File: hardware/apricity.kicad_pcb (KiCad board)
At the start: 2 copper layers, 71.2 x 71.2 mm, 26 parts, among them J1 USB_C_Receptacle_USB2.0, U1 ESP-WROOM-02D, U2 X

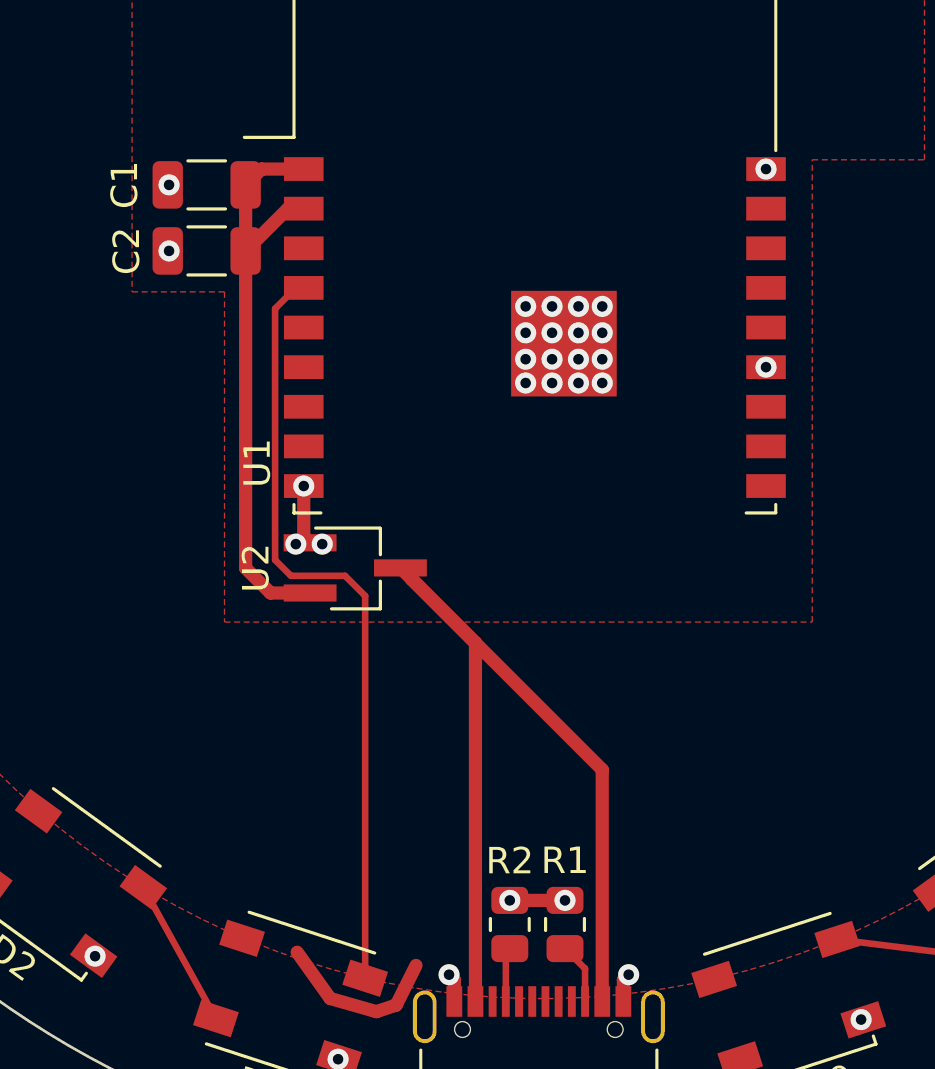
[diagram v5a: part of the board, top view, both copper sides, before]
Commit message: remove vias from under pads
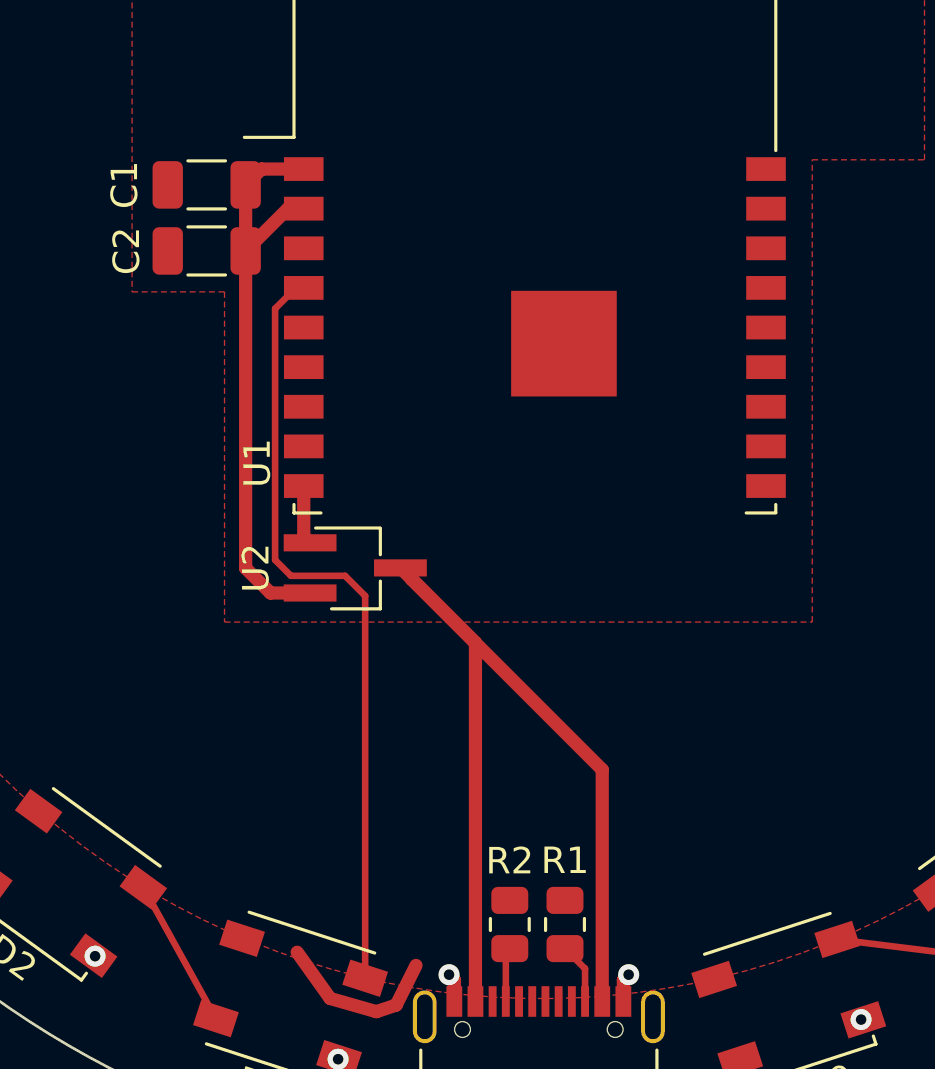
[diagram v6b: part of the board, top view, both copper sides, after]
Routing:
- net GND: track 6.54 -> 4.45 mm, vias 46 -> 21
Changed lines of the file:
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@@
   )
   (segment (start 139 103.6) (end 139 105.51) (width 0.5) (layer "F.Cu") (net 1))
-  (segment (start 146.8 119.2875) (end 148.89 119.2875) (width 0.5) (layer "F.Cu") (net 1))
   (segment (start 144.7 122.3) (end 144.5 122.1) (width 0.5) (layer "F.Cu") (net 1))
   (segment (start 151.1 122.3) (end 151.3 122.1) (width 0.5) (layer "F.Cu") (net 1))
@@
   (segment (start 139 105.51) (end 139.24 105.75) (width 0.5) (layer "F.Cu") (net 1))
   (via (at 155.7 62.7) (size 0.8) (drill 0.4) (layers "F.Cu" "B.Cu") (net 1))
-  (via (at 150.3 96.8) (size 0.8) (drill 0.4) (layers "F.Cu" "B.Cu") (net 1))
-  (via (at 147.4 98.8) (size 0.8) (drill 0.4) (layers "F.Cu" "B.Cu") (net 1))
-  (via (at 148.4 96.8) (size 0.8) (drill 0.4) (layers "F.Cu" "B.Cu") (net 1))
   (via (at 144.5 122.1) (size 0.8) (drill 0.4) (layers "F.Cu" "B.Cu") (free) (net 1))
-  (via (at 147.4 96.8) (size 0.8) (drill 0.4) (layers "F.Cu" "B.Cu") (net 1))
-  (via (at 150.3 97.8) (size 0.8) (drill 0.4) (layers "F.Cu" "B.Cu") (net 1))
   (via (at 135.8 64.2) (size 0.8) (drill 0.4) (layers "F.Cu" "B.Cu") (net 1))
-  (via (at 150.3 98.8) (size 0.8) (drill 0.4) (layers "F.Cu" "B.Cu") (net 1))
   (via (at 177.8 81.8) (size 0.8) (drill 0.4) (layers "F.Cu" "B.Cu") (net 1))
   (via (at 172.6 73.2) (size 0.8) (drill 0.4) (layers "F.Cu" "B.Cu") (net 1))
   (via (at 179.3 101.7) (size 0.8) (drill 0.4) (layers "F.Cu" "B.Cu") (net 1))
-  (via (at 133.9 94.7) (size 0.8) (drill 0.4) (layers "F.Cu" "B.Cu") (net 1))
-  (via (at 146.8 119.2875) (size 0.8) (drill 0.4) (layers "F.Cu" "B.Cu") (net 1))
-  (via (at 156.5 91.6) (size 0.8) (drill 0.4) (layers "F.Cu" "B.Cu") (net 1))
   (via (at 165 66.6) (size 0.8) (drill 0.4) (layers "F.Cu" "B.Cu") (net 1))
-  (via (at 133.9 92.2) (size 0.8) (drill 0.4) (layers "F.Cu" "B.Cu") (net 1))
-  (via (at 149.4 97.8) (size 0.8) (drill 0.4) (layers "F.Cu" "B.Cu") (net 1))
   (via (at 118.2 106.3) (size 0.8) (drill 0.4) (layers "F.Cu" "B.Cu") (net 1))
   (via (at 127.2 69.4) (size 0.8) (drill 0.4) (layers "F.Cu" "B.Cu") (net 1))
-  (via (at 139.7 105.8) (size 0.8) (drill 0.4) (layers "F.Cu" "B.Cu") (net 1))
   (via (at 168.8 118.6) (size 0.8) (drill 0.4) (layers "F.Cu" "B.Cu") (net 1))
   (via (at 145.6 61.9) (size 0.8) (drill 0.4) (layers "F.Cu" "B.Cu") (net 1))
-  (via (at 148.4 97.8) (size 0.8) (drill 0.4) (layers "F.Cu" "B.Cu") (net 1))
-  (via (at 148.89 119.2875) (size 0.8) (drill 0.4) (layers "F.Cu" "B.Cu") (net 1))
-  (via (at 139 103.6) (size 0.8) (drill 0.4) (layers "F.Cu" "B.Cu") (net 1))
-  (via (at 147.4 99.7) (size 0.8) (drill 0.4) (layers "F.Cu" "B.Cu") (net 1))
   (via (at 115.9 96.4) (size 0.8) (drill 0.4) (layers "F.Cu" "B.Cu") (net 1))
-  (via (at 148.4 98.8) (size 0.8) (drill 0.4) (layers "F.Cu" "B.Cu") (net 1))
   (via (at 151.3 122.1) (size 0.8) (drill 0.4) (layers "F.Cu" "B.Cu") (free) (net 1))
   (via (at 131.1 121.4) (size 0.8) (drill 0.4) (layers "F.Cu" "B.Cu") (net 1))
   (via (at 116.7 86.4) (size 0.8) (drill 0.4) (layers "F.Cu" "B.Cu") (net 1))
-  (via (at 150.3 99.7) (size 0.8) (drill 0.4) (layers "F.Cu" "B.Cu") (net 1))
   (via (at 175.4 111) (size 0.8) (drill 0.4) (layers "F.Cu" "B.Cu") (net 1))
-  (via (at 138.7 105.8) (size 0.8) (drill 0.4) (layers "F.Cu" "B.Cu") (net 1))
-  (via (at 148.4 99.7) (size 0.8) (drill 0.4) (layers "F.Cu" "B.Cu") (net 1))
-  (via (at 149.4 96.8) (size 0.8) (drill 0.4) (layers "F.Cu" "B.Cu") (net 1))
   (via (at 160.1 123.8) (size 0.8) (drill 0.4) (layers "F.Cu" "B.Cu") (net 1))
   (via (at 140.3 125.3) (size 0.8) (drill 0.4) (layers "F.Cu" "B.Cu") (net 1))
-  (via (at 147.4 97.8) (size 0.8) (drill 0.4) (layers "F.Cu" "B.Cu") (net 1))
   (via (at 120.6 77) (size 0.8) (drill 0.4) (layers "F.Cu" "B.Cu") (net 1))
-  (via (at 156.5 99.1) (size 0.8) (drill 0.4) (layers "F.Cu" "B.Cu") (net 1))
-  (via (at 149.4 98.8) (size 0.8) (drill 0.4) (layers "F.Cu" "B.Cu") (net 1))
   (via (at 180.1 91.6) (size 0.8) (drill 0.4) (layers "F.Cu" "B.Cu") (net 1))
-  (via (at 149.4 99.7) (size 0.8) (drill 0.4) (layers "F.Cu" "B.Cu") (net 1))
   (via (at 123.4 114.8) (size 0.8) (drill 0.4) (layers "F.Cu" "B.Cu") (net 1))
   (segment (start 150.3 123.115) (end 150.3 114.34) (width 0.5) (layer "F.Cu") (net 2))

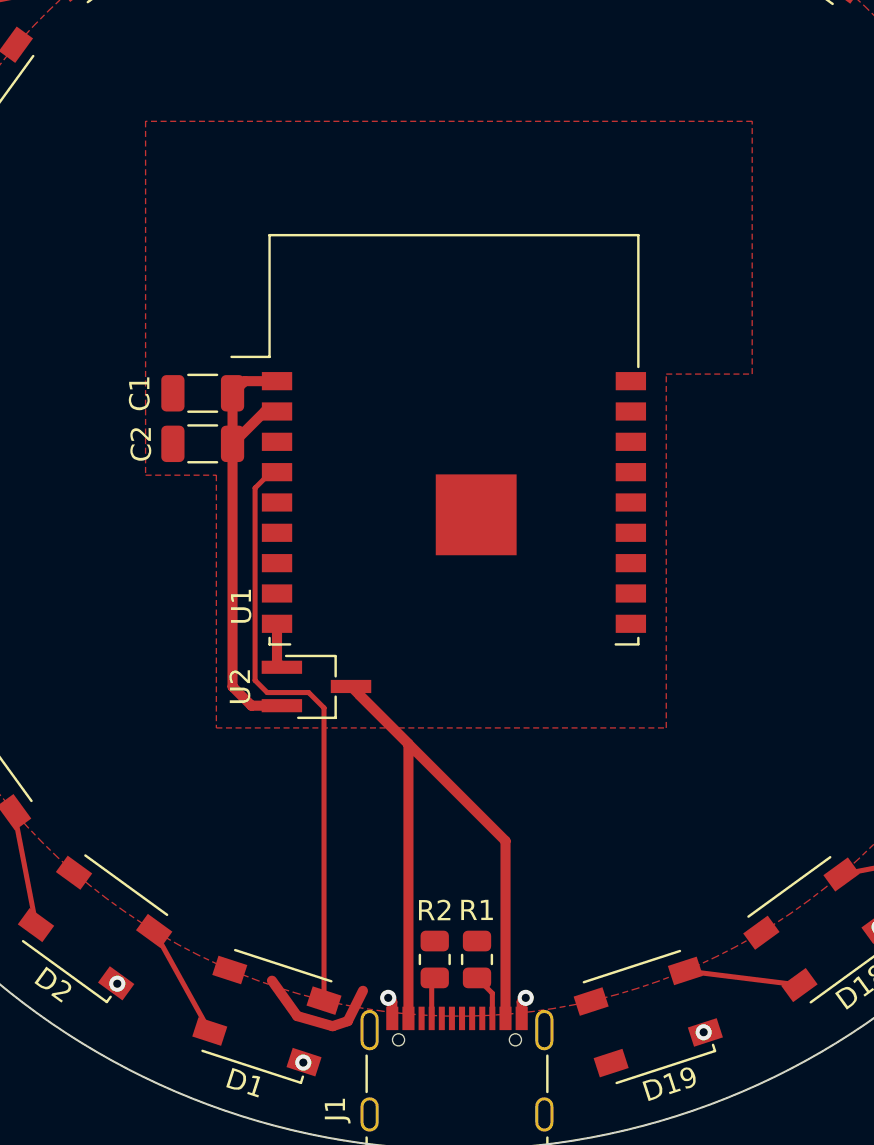
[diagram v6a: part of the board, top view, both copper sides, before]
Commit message: reintroduce ground plane below controller
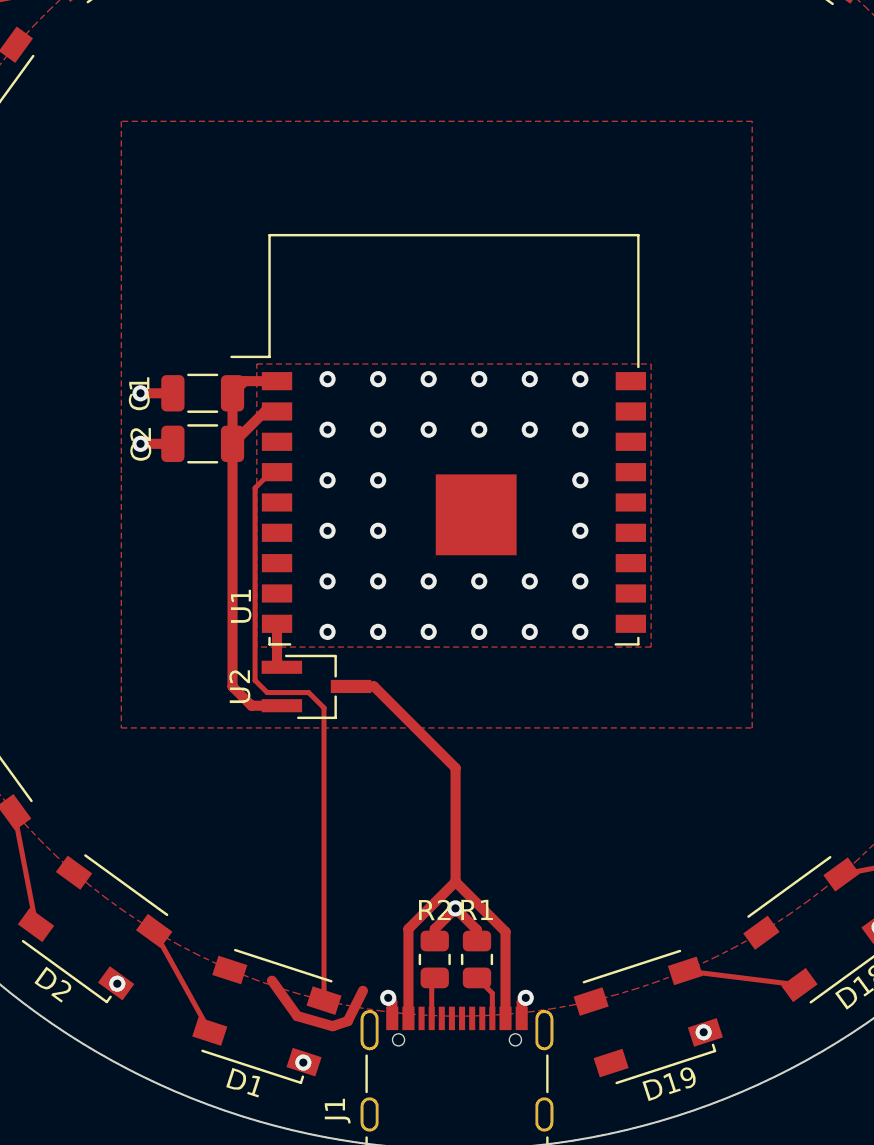
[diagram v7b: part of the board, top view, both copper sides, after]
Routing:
- net +5V: track 43.0 -> 34.4 mm
- net GND: track 4.45 -> 11.7 mm, vias 21 -> 54
- added copper zone on F.Cu, net GND
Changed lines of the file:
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@@
   )
   (segment (start 139 103.6) (end 139 105.51) (width 0.5) (layer "F.Cu") (net 1))
+  (segment (start 133.85 92.2) (end 132.25 92.2) (width 0.5) (layer "F.Cu") (net 1))
+  (segment (start 133.85 94.7) (end 132.25 94.7) (width 0.5) (layer "F.Cu") (net 1))
+  (segment (start 146.8 118.7) (end 147.825 117.675) (width 0.5) (layer "F.Cu") (net 1))
+  (segment (start 148.89 119.2875) (end 148.89 118.74) (width 0.5) (layer "F.Cu") (net 1))
   (segment (start 144.7 122.3) (end 144.5 122.1) (width 0.5) (layer "F.Cu") (net 1))
+  (segment (start 148.89 118.74) (end 147.825 117.675) (width 0.5) (layer "F.Cu") (net 1))
+  (segment (start 146.8 119.2875) (end 146.8 118.7) (width 0.5) (layer "F.Cu") (net 1))
   (segment (start 151.1 122.3) (end 151.3 122.1) (width 0.5) (layer "F.Cu") (net 1))
   (segment (start 151.1 123.115) (end 151.1 122.3) (width 0.5) (layer "F.Cu") (net 1))
@@
   (segment (start 139 105.51) (end 139.24 105.75) (width 0.5) (layer "F.Cu") (net 1))
   (via (at 155.7 62.7) (size 0.8) (drill 0.4) (layers "F.Cu" "B.Cu") (net 1))
+  (via (at 147.825 117.675) (size 0.8) (drill 0.4) (layers "F.Cu" "B.Cu") (free) (net 1))
+  (via (at 154 99) (size 0.8) (drill 0.4) (layers "F.Cu" "B.Cu") (free) (net 1))
+  (via (at 146.5 94) (size 0.8) (drill 0.4) (layers "F.Cu" "B.Cu") (free) (net 1))
+  (via (at 149 101.5) (size 0.8) (drill 0.4) (layers "F.Cu" "B.Cu") (free) (net 1))
+  (via (at 132.25 92.2) (size 0.8) (drill 0.4) (layers "F.Cu" "B.Cu") (free) (net 1))
+  (via (at 149 94) (size 0.8) (drill 0.4) (layers "F.Cu" "B.Cu") (free) (net 1))
+  (via (at 144 94) (size 0.8) (drill 0.4) (layers "F.Cu" "B.Cu") (free) (net 1))
+  (via (at 144 101.5) (size 0.8) (drill 0.4) (layers "F.Cu" "B.Cu") (free) (net 1))
   (via (at 144.5 122.1) (size 0.8) (drill 0.4) (layers "F.Cu" "B.Cu") (free) (net 1))
   (via (at 135.8 64.2) (size 0.8) (drill 0.4) (layers "F.Cu" "B.Cu") (net 1))
+  (via (at 151.5 101.5) (size 0.8) (drill 0.4) (layers "F.Cu" "B.Cu") (free) (net 1))
   (via (at 177.8 81.8) (size 0.8) (drill 0.4) (layers "F.Cu" "B.Cu") (net 1))
   (via (at 172.6 73.2) (size 0.8) (drill 0.4) (layers "F.Cu" "B.Cu") (net 1))
   (via (at 179.3 101.7) (size 0.8) (drill 0.4) (layers "F.Cu" "B.Cu") (net 1))
   (via (at 165 66.6) (size 0.8) (drill 0.4) (layers "F.Cu" "B.Cu") (net 1))
+  (via (at 151.5 91.5) (size 0.8) (drill 0.4) (layers "F.Cu" "B.Cu") (free) (net 1))
+  (via (at 154 94) (size 0.8) (drill 0.4) (layers "F.Cu" "B.Cu") (free) (net 1))
   (via (at 118.2 106.3) (size 0.8) (drill 0.4) (layers "F.Cu" "B.Cu") (net 1))
   (via (at 127.2 69.4) (size 0.8) (drill 0.4) (layers "F.Cu" "B.Cu") (net 1))
+  (via (at 146.5 104) (size 0.8) (drill 0.4) (layers "F.Cu" "B.Cu") (free) (net 1))
+  (via (at 154 101.5) (size 0.8) (drill 0.4) (layers "F.Cu" "B.Cu") (free) (net 1))
   (via (at 168.8 118.6) (size 0.8) (drill 0.4) (layers "F.Cu" "B.Cu") (net 1))
   (via (at 145.6 61.9) (size 0.8) (drill 0.4) (layers "F.Cu" "B.Cu") (net 1))
+  (via (at 154 104) (size 0.8) (drill 0.4) (layers "F.Cu" "B.Cu") (free) (net 1))
+  (via (at 141.5 96.5) (size 0.8) (drill 0.4) (layers "F.Cu" "B.Cu") (free) (net 1))
+  (via (at 144 104) (size 0.8) (drill 0.4) (layers "F.Cu" "B.Cu") (free) (net 1))
+  (via (at 151.5 94) (size 0.8) (drill 0.4) (layers "F.Cu" "B.Cu") (free) (net 1))
+  (via (at 141.5 91.5) (size 0.8) (drill 0.4) (layers "F.Cu" "B.Cu") (free) (net 1))
+  (via (at 132.25 94.7) (size 0.8) (drill 0.4) (layers "F.Cu" "B.Cu") (free) (net 1))
   (via (at 115.9 96.4) (size 0.8) (drill 0.4) (layers "F.Cu" "B.Cu") (net 1))
+  (via (at 149 91.5) (size 0.8) (drill 0.4) (layers "F.Cu" "B.Cu") (free) (net 1))
+  (via (at 146.5 101.5) (size 0.8) (drill 0.4) (layers "F.Cu" "B.Cu") (free) (net 1))
   (via (at 151.3 122.1) (size 0.8) (drill 0.4) (layers "F.Cu" "B.Cu") (free) (net 1))
   (via (at 131.1 121.4) (size 0.8) (drill 0.4) (layers "F.Cu" "B.Cu") (net 1))
   (via (at 116.7 86.4) (size 0.8) (drill 0.4) (layers "F.Cu" "B.Cu") (net 1))
+  (via (at 144 99) (size 0.8) (drill 0.4) (layers "F.Cu" "B.Cu") (free) (net 1))
   (via (at 175.4 111) (size 0.8) (drill 0.4) (layers "F.Cu" "B.Cu") (net 1))
+  (via (at 144 96.5) (size 0.8) (drill 0.4) (layers "F.Cu" "B.Cu") (free) (net 1))
+  (via (at 144 91.5) (size 0.8) (drill 0.4) (layers "F.Cu" "B.Cu") (free) (net 1))
+  (via (at 149 104) (size 0.8) (drill 0.4) (layers "F.Cu" "B.Cu") (free) (net 1))
+  (via (at 154 96.5) (size 0.8) (drill 0.4) (layers "F.Cu" "B.Cu") (free) (net 1))
   (via (at 160.1 123.8) (size 0.8) (drill 0.4) (layers "F.Cu" "B.Cu") (net 1))
+  (via (at 141.5 99) (size 0.8) (drill 0.4) (layers "F.Cu" "B.Cu") (free) (net 1))
   (via (at 140.3 125.3) (size 0.8) (drill 0.4) (layers "F.Cu" "B.Cu") (net 1))
   (via (at 120.6 77) (size 0.8) (drill 0.4) (layers "F.Cu" "B.Cu") (net 1))
+  (via (at 151.5 104) (size 0.8) (drill 0.4) (layers "F.Cu" "B.Cu") (free) (net 1))
+  (via (at 154 91.5) (size 0.8) (drill 0.4) (layers "F.Cu" "B.Cu") (free) (net 1))
   (via (at 180.1 91.6) (size 0.8) (drill 0.4) (layers "F.Cu" "B.Cu") (net 1))
+  (via (at 141.5 104) (size 0.8) (drill 0.4) (layers "F.Cu" "B.Cu") (free) (net 1))
+  (via (at 141.5 94) (size 0.8) (drill 0.4) (layers "F.Cu" "B.Cu") (free) (net 1))
   (via (at 123.4 114.8) (size 0.8) (drill 0.4) (layers "F.Cu" "B.Cu") (net 1))
-  (segment (start 150.3 123.115) (end 150.3 114.34) (width 0.5) (layer "F.Cu") (net 2))
-  (segment (start 143.08 107.12) (end 142.66 106.7) (width 0.5) (layer "F.Cu") (net 2))
-  (segment (start 150.3 114.34) (end 143.08 107.12) (width 0.5) (layer "F.Cu") (net 2))
+  (via (at 146.5 91.5) (size 0.8) (drill 0.4) (layers "F.Cu" "B.Cu") (free) (net 1))
+  (via (at 141.5 101.5) (size 0.8) (drill 0.4) (layers "F.Cu" "B.Cu") (free) (net 1))
+  (segment (start 145.5 118.69) (end 147.83 116.36) (width 0.5) (layer "F.Cu") (net 2))
+  (segment (start 147.83 116.36) (end 150.3 118.83) (width 0.5) (layer "F.Cu") (net 2))
+  (segment (start 145.5 123.115) (end 145.5 118.69) (width 0.5) (layer "F.Cu") (net 2))
+  (segment (start 150.3 118.83) (end 150.3 123.115) (width 0.5) (layer "F.Cu") (net 2))
   (segment (start 143.25 121.75) (end 142.5 123.25) (width 0.5) (layer "F.Cu") (net 2))
-  (segment (start 145.5 109.54) (end 143.08 107.12) (width 0.5) (layer "F.Cu") (net 2))
+  (segment (start 147.83 116.36) (end 147.83 110.73) (width 0.5) (layer "F.Cu") (net 2))
+  (segment (start 147.83 110.73) (end 143.8 106.7) (width 0.5) (layer "F.Cu") (net 2))
   (segment (start 140 123) (end 138.75 121.25) (width 0.5) (layer "F.Cu") (net 2))
-  (segment (start 145.5 123.115) (end 145.5 109.54) (width 0.5) (layer "F.Cu") (net 2))
   (segment (start 141.75 123.5) (end 140 123) (width 0.5) (layer "F.Cu") (net 2))
+  (segment (start 143.8 106.7) (end 142.66 106.7) (width 0.5) (layer "F.Cu") (net 2))
   (segment (start 142.5 123.25) (end 141.75 123.5) (width 0.5) (layer "F.Cu") (net 2))
   (segment (start 140.565 107) (end 141.324516 107.759516) (width 0.25) (layer "F.Cu") (net 3))
@@
     (polygon
       (pts
-        (xy 132.5 78.75)
-        (xy 132.5 96.25)
-        (xy 136 96.25)
-        (xy 136 108.75)
-        (xy 158.25 108.75)
-        (xy 158.25 91.25)
-        (xy 162.5 91.25)
+        (xy 131.3 78.75)
+        (xy 131.3 96.25)
+        (xy 131.3 108.75)
+        (xy 162.5 108.75)
         (xy 162.5 78.75)
       )
     )
+  )
+  (zone (net 1) (net_name "GND") (layer "F.Cu") (hatch edge 0.508)
+    (connect_pads (clearance 0.508))
+    (min_thickness 0.254) (filled_areas_thickness no)
+    (fill yes (thermal_gap 0.508) (thermal_bridge_width 0.508))
+    (polygon
+      (pts
+        (xy 157.5 104.75)
+        (xy 138 104.75)
+        (xy 138 90.75)
+        (xy 157.5 90.75)
+      )
+    )
